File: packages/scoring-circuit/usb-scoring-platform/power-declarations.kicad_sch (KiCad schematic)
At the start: 0 parts

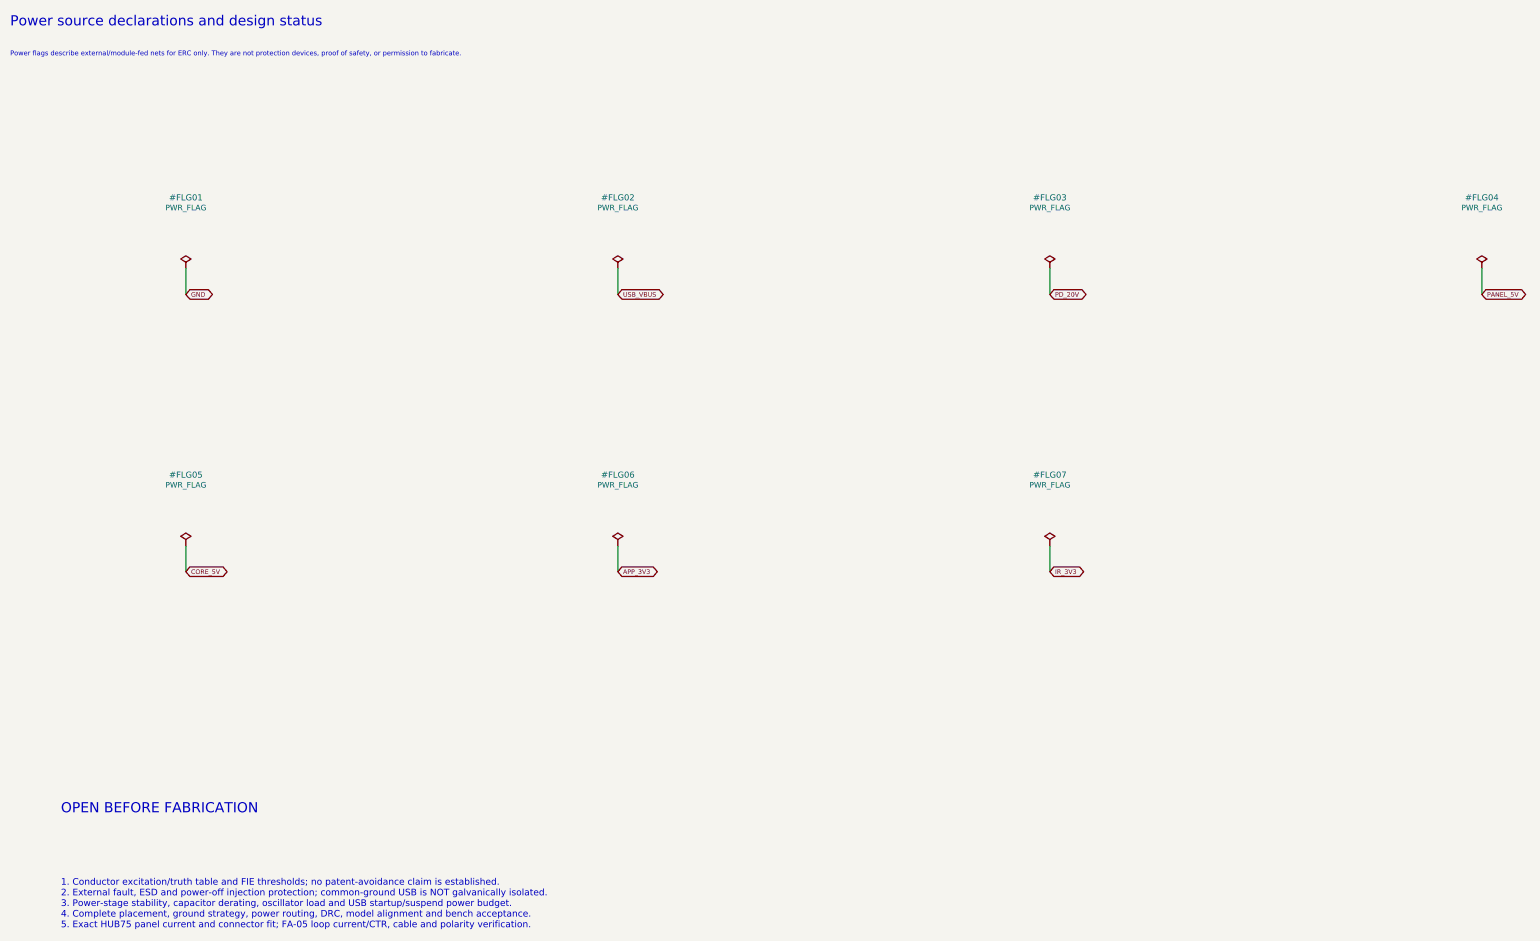
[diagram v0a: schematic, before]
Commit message: feat(scoring-circuit): isolate computer USB in native KiCad draft
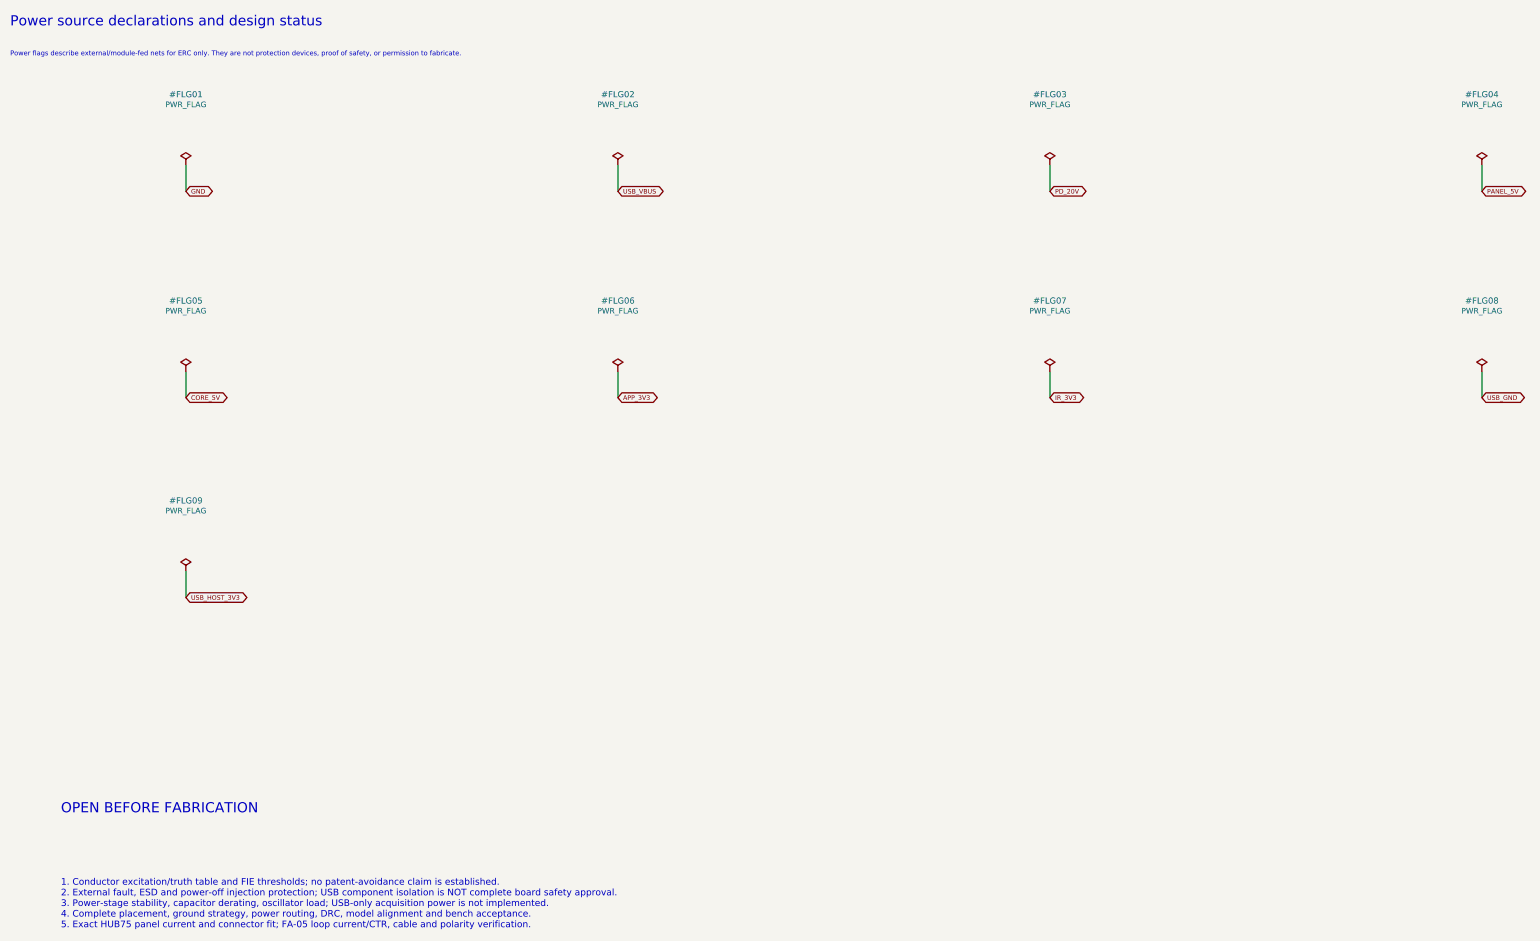
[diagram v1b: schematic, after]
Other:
- note added: "1. Conductor excitation/truth table and FIE thresholds; no patent-avoidance claim is established. 2. External fault, ESD and power-off injection protection; USB component isolation is NOT complete board safety approval. 3. Power-stage stability, capacitor derating, oscillator load; USB-only acquisition power is not implemented. 4. Complete placement, ground strategy, power routing, DRC, model ali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"
- note removed: "1. Conductor excitation/truth table and FIE thresholds; no patent-avoidance claim is established. 2. External fault, ESD and power-off injection protection; common-ground USB is NOT galvanically isolated. 3. Power-stage stability, capacitor derating, oscillator load and USB startup/suspend power budget. 4. Complete placement, ground strategy, power routing, DRC, model alignment and bench acceptan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"

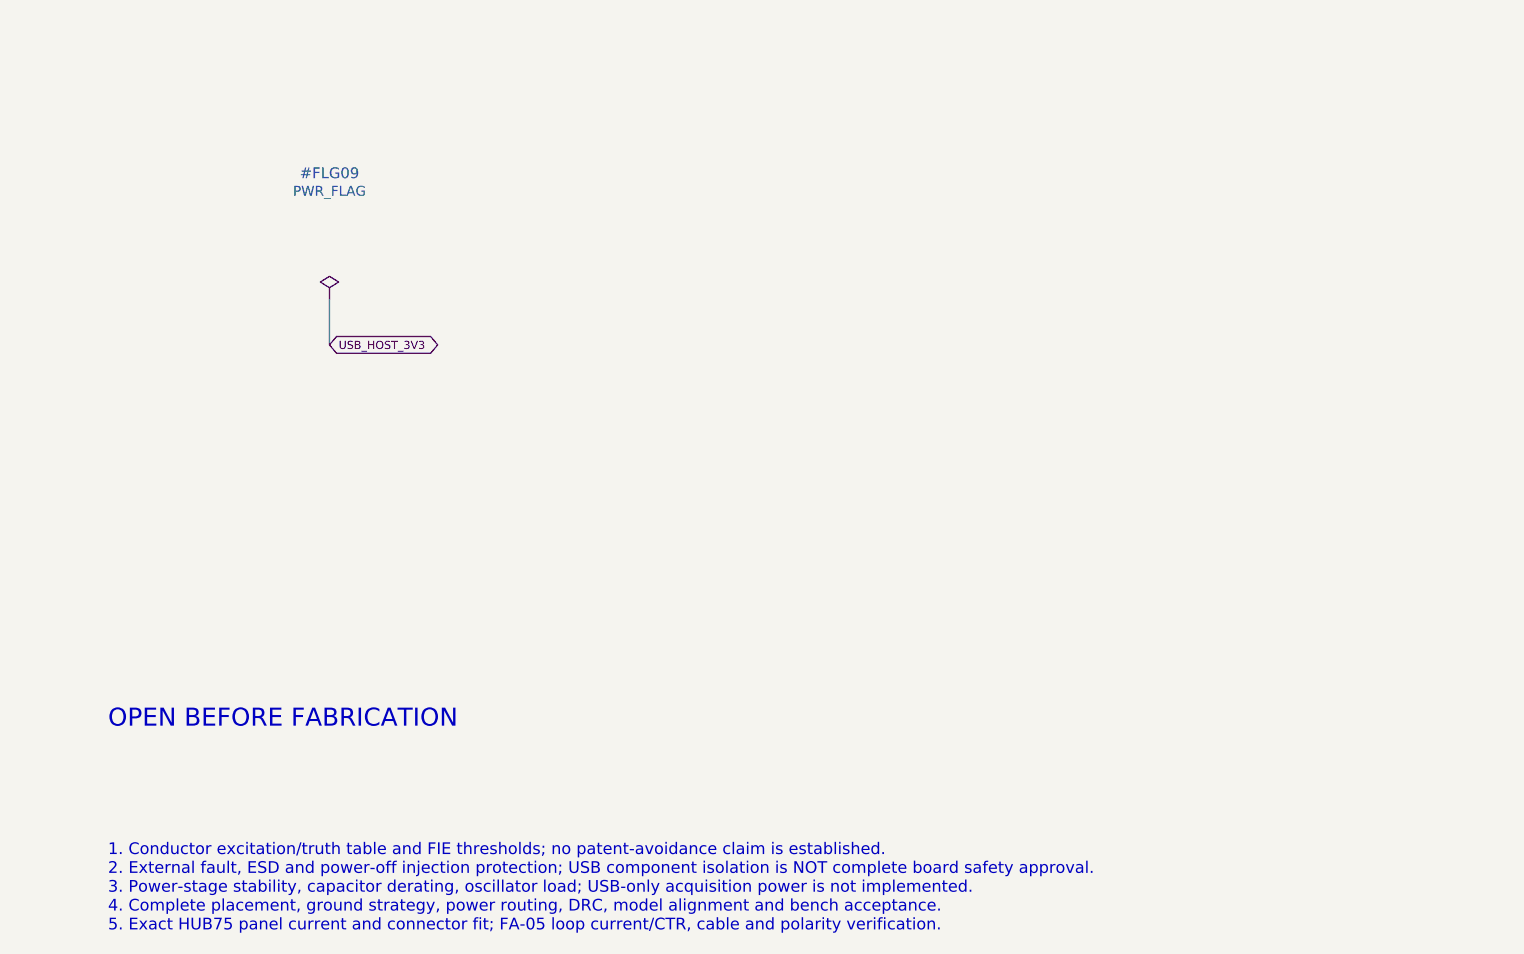
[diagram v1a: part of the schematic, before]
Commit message: feat(scoring-circuit): add isolated single-cable USB acquisition power
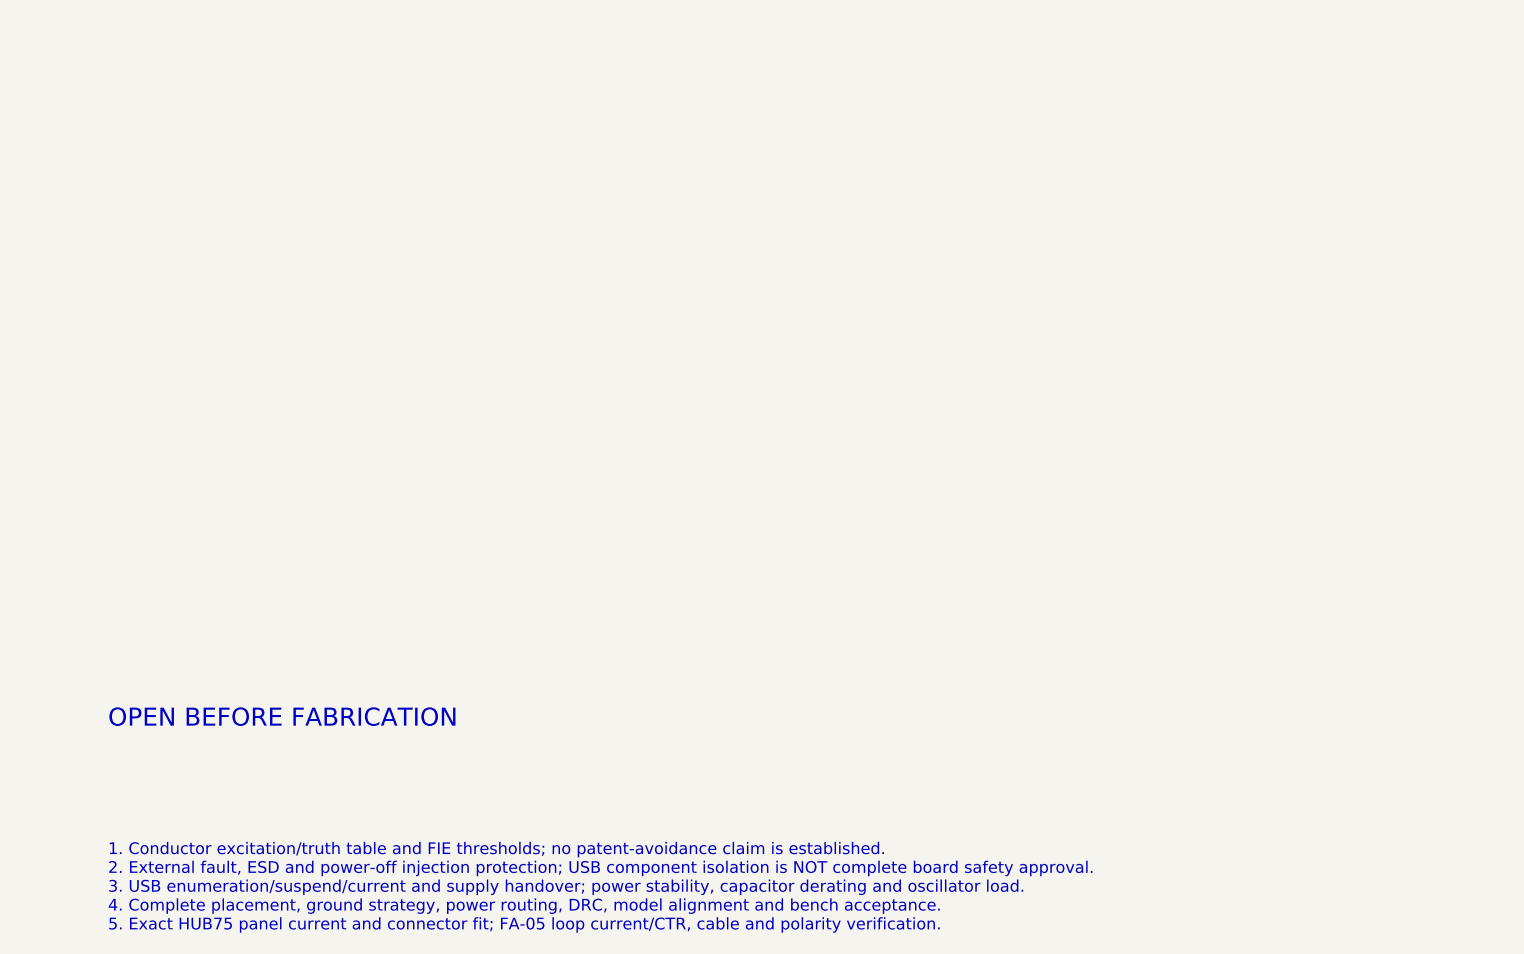
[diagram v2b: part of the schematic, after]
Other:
- note added: "1. Conductor excitation/truth table and FIE thresholds; no patent-avoidance claim is established. 2. External fault, ESD and power-off injection protection; USB component isolation is NOT complete board safety approval. 3. USB enumeration/suspend/current and supply handover; power stability, capacitor derating and oscillator load. 4. Complete placement, ground strategy, power routing, DRC, model 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"
- note removed: "1. Conductor excitation/truth table and FIE thresholds; no patent-avoidance claim is established. 2. External fault, ESD and power-off injection protection; USB component isolation is NOT complete board safety approval. 3. Power-stage stability, capacitor derating, oscillator load; USB-only acquisition power is not implemented. 4. Complete placement, ground strategy, power routing, DRC, model ali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"
